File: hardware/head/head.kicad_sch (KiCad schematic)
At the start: 68 parts, among them J1 Head bundle, J10 CM4 socket 101-200, J11 Ext amp, J12 Ext 5V, J13 SPI pads, J2 ToF, J3 I2C breakout, J4 Eye LED, J5 Speaker, J6 Fan, J7 Microphone, J8 Camera, J9 CM4 socket 1-100, Q1 AO3400A, U2 LMR51635YDDCR, U3 AMS1117-3.3, U4 MAX98357AETE+T, U5 BMI088

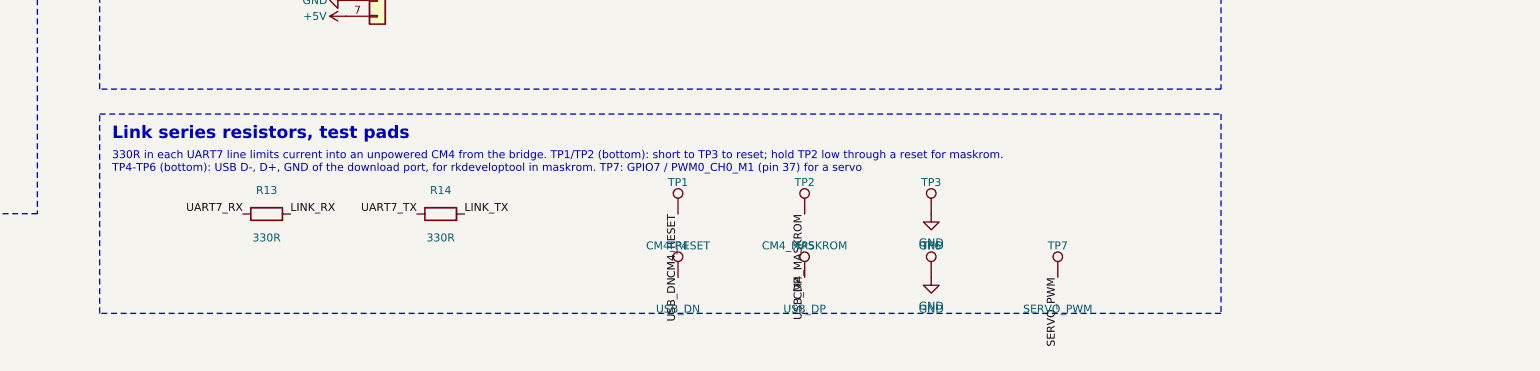
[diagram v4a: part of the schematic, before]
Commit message: Head PCB: rev B second review, head_ext variant with the BMI088 module
Rev B (hardware/head), second pre-order review (docs/head-pcb.md 9.5):
- R13 1k on the link RX line; J13's 5 V re-routed clear of the module
  hole; ground vias and solid ground pads at C1, C2, D1 and C17; 3.3 V
  copper on the AMS1117 tab
- CM4 orientation marks (CM4 U.FL END, pin 1 and 101 dots); J11 and J12
  names on the back
- polarity picture for JLC's placement preview

head_ext (hardware/head_ext, 9.6): rev B with the generic BMI088 module
hand-fitted in place of the chip, so the board needs only Economic PCBA
- U5 chip, C15, C16, JP4, JP5, R8, R9 and the J3 PH header removed
- module on the front, rows 11.3 mm apart; I2C8 pins (J3, 2.0 mm) and
  J12 on the right edge; J11 as bottom-side solder pads
- pin names on both sides; re-routed locally with Freerouting and the
  maze router; DRC clean with schematic parity
- reviewed against rev B: netlist, rev B's fixes, re-routed nets, silk,
  JLC stock

Placement: export_jlc.py now corrects the CPL rotation (and origin)
where JLC's EasyEDA footprint is turned from ours: the DF40C sockets,
SOT-23, SOT-23-6, SOT-223, TQFN-16 and LGA-16 on the head boards, and
the bridge's hand fixes of a4dfda9, which it now reproduces.

Tools: gen_head_sch.py --variant head_ext, sync_head_pcb.py --board and
--prune, make_head_ext_pcb.py, rip_under_pads.py, nudge_fp.py; tidy,
finish and polarity scripts take the board name; undangle keeps a via
inside a same-net pad.
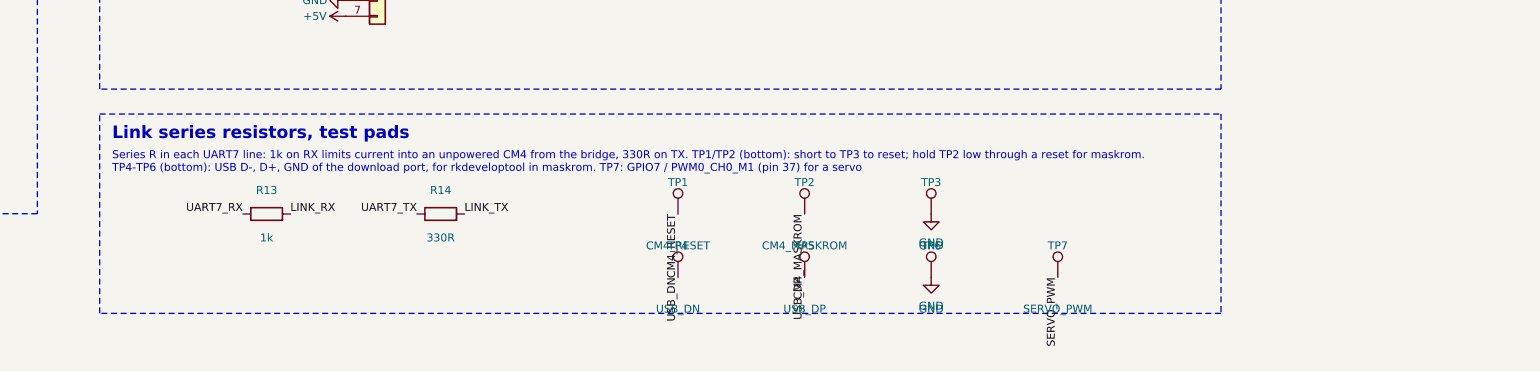
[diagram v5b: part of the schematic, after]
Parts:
- R13: value 330R -> 1k; LCSC C23138 -> C21190
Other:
- note added: "Series R in each UART7 line: 1k on RX limits current into an unpowered CM4 from the bridge, 330R on TX. TP1/TP2 (bottom): short to TP3 to reset; hold TP2 low through a reset for maskrom. TP4-TP6 (bottom): USB D-, D+, GND of the download port, for rkdeveloptool in maskrom. TP7: GPIO7 / PWM0_CH0_M1 (pin 37) for a servo"
- note removed: "330R in each UART7 line limits current into an unpowered CM4 from the bridge. TP1/TP2 (bottom): short to TP3 to reset; hold TP2 low through a reset for maskrom. TP4-TP6 (bottom): USB D-, D+, GND of the download port, for rkdeveloptool in maskrom. TP7: GPIO7 / PWM0_CH0_M1 (pin 37) for a servo"
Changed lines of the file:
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@@
   (text "Link series resistors, test pads" (exclude_from_sim no) (at 407 386 0)
     (effects (font (size 2.0 2.0) bold) (justify left top)))
-  (text "330R in each UART7 line limits current into an unpowered CM4 from the bridge. TP1/TP2 (bottom): short to TP3 to reset; hold TP2 low through a reset for maskrom.\nTP4-TP6 (bottom): USB D-, D+, GND of the download port, for rkdeveloptool in maskrom. TP7: GPIO7 / PWM0_CH0_M1 (pin 37) for a servo" (exclude_from_sim no) (at 407 390 0)
+  (text "Series R in each UART7 line: 1k on RX limits current into an unpowered CM4 from the bridge, 330R on TX. TP1/TP2 (bottom): short to TP3 to reset; hold TP2 low through a reset for maskrom.\nTP4-TP6 (bottom): USB D-, D+, GND of the download port, for rkdeveloptool in maskrom. TP7: GPIO7 / PWM0_CH0_M1 (pin 37) for a servo" (exclude_from_sim no) (at 407 390 0)
     (effects (font (size 1.27 1.27)) (justify left top)))
   (symbol (lib_id "Device:R") (at 431.8 400.05 90) (unit 1)
@@
     (property "Reference" "R13" (at 431.8 396.24 90)
       (effects (font (size 1.27 1.27))))
-    (property "Value" "330R" (at 431.8 403.86 90)
+    (property "Value" "1k" (at 431.8 403.86 90)
       (effects (font (size 1.27 1.27))))
     (property "Footprint" "Resistor_SMD:R_0603_1608Metric" (at 431.8 400.05 90)
@@
     (property "Description" "" (at 431.8 400.05 90)
       (effects (font (size 1.27 1.27)) (hide yes)))
-    (property "LCSC" "C23138" (at 431.8 400.05 90)
+    (property "LCSC" "C21190" (at 431.8 400.05 90)
       (effects (font (size 1.27 1.27)) (hide yes)))
     (pin "1")
